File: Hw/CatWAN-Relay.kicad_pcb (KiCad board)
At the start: 2 copper layers, 50 x 86.9 mm, 55 parts, among them J2 INPUTS, J3 OUTPUTS, J4 I2C, J5 Serial, P1 USB_C_Plug_USB2.0, Q1 MMBT2222A, Q2 MMBT2222A, Q3 MMBT2222A, SW1 BOOT, SW2 RESET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

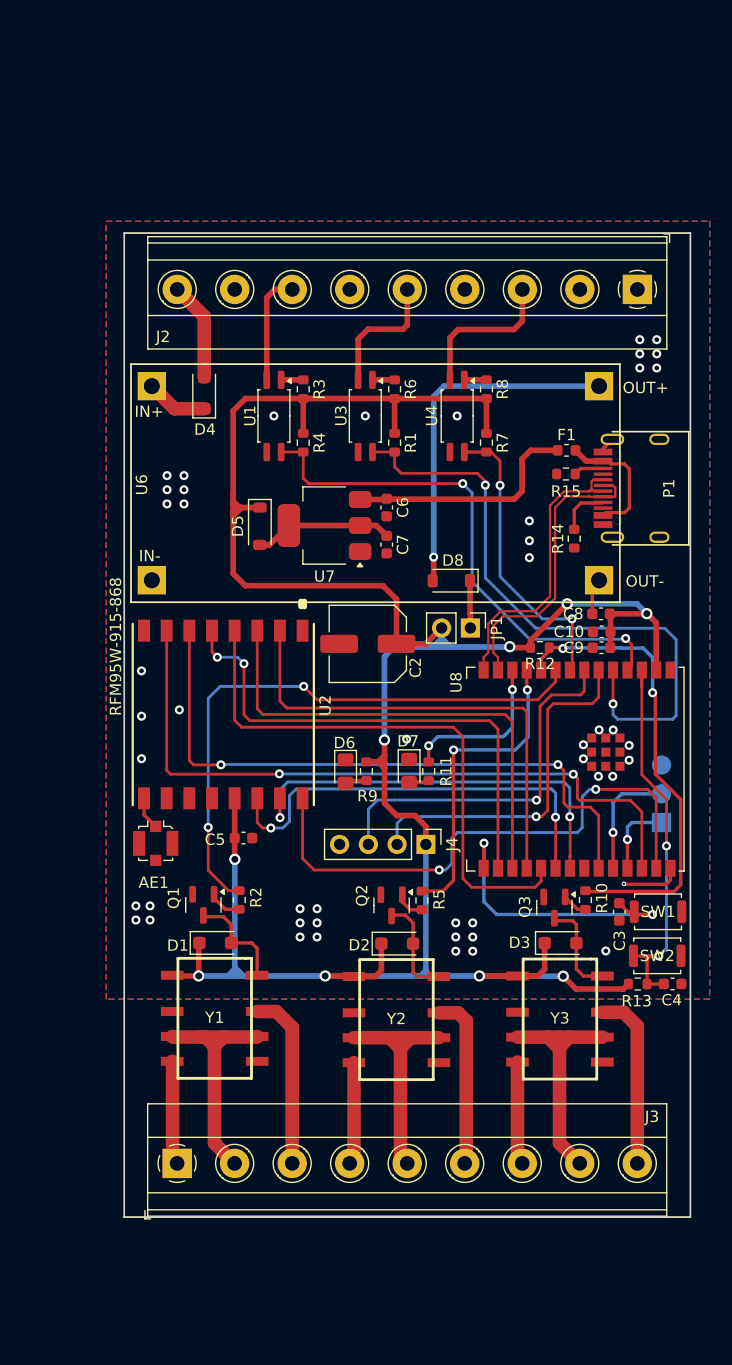
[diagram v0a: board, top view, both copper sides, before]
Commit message: feat(hw): add labels in PCB design
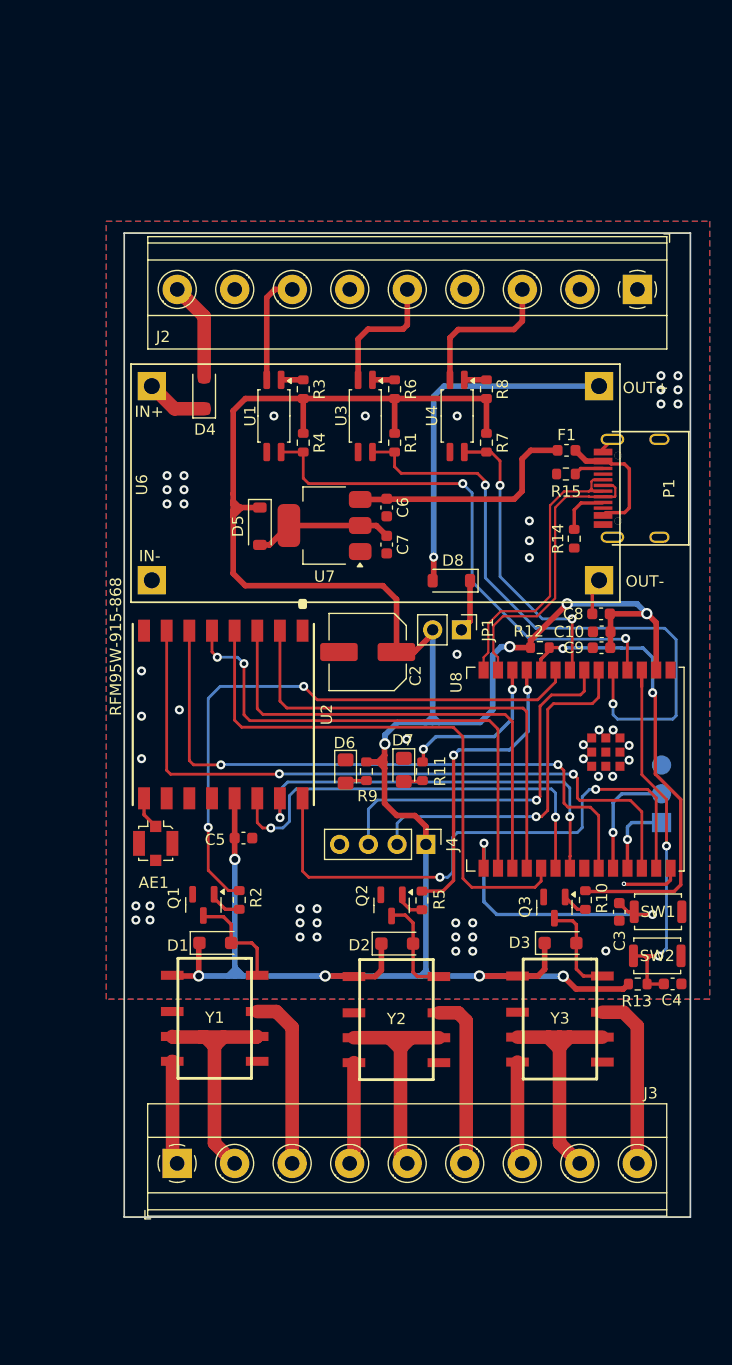
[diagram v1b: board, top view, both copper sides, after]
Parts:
- added G***: LOGO, agroin:electronic_cats_logo_8x6, B.Cu at (55.7, 67.0)
- added kibuzzard-67649598: G***, kibuzzard-67649598, B.Cu at (85.9, 89.6)
- added kibuzzard-676495AB: G***, kibuzzard-676495AB, B.Cu at (85.9, 87.1)
- added kibuzzard-676D7180: G***, kibuzzard-676D7180, B.Cu at (85.6, 84.6)
- added kibuzzard-676D7534: G***, kibuzzard-676D7534, B.Cu at (79.7, 51.0)
- added kibuzzard-676D753C: G***, kibuzzard-676D753C, B.Cu at (79.5, 68.1)
- added kibuzzard-676D7543: G***, kibuzzard-676D7543, B.Cu at (47.2, 68.2)
- added kibuzzard-676D7549: G***, kibuzzard-676D7549, B.Cu at (47.2, 51.2)
- added kibuzzard-676D7550: G***, kibuzzard-676D7550, B.Cu at (46.1, 115.3)
- added kibuzzard-676D7558: G***, kibuzzard-676D7558, B.Cu at (51.2, 115.0)
- added kibuzzard-676D7562: G***, kibuzzard-676D7562, B.Cu at (56.2, 115.3)
- added kibuzzard-676D7567: G***, kibuzzard-676D7567, B.Cu at (61.3, 115.3)
- added kibuzzard-676D757C: G***, kibuzzard-676D757C, B.Cu at (71.6, 115.3)
- added kibuzzard-676D7581: G***, kibuzzard-676D7581, B.Cu at (76.7, 115.3)
- added kibuzzard-676D758E: G***, kibuzzard-676D758E, B.Cu at (86.9, 115.3)
- added kibuzzard-676D75AF: G***, kibuzzard-676D75AF, B.Cu at (66.4, 114.8)
- added kibuzzard-676D75BA: G***, kibuzzard-676D75BA, B.Cu at (81.8, 114.8)
- added kibuzzard-676D829F: G***, kibuzzard-676D829F, B.Cu at (62.0, 67.0)
- added kibuzzard-676D82E6: G***, kibuzzard-676D82E6, B.Cu at (46.1, 47.0)
- added kibuzzard-676D82FB: G***, kibuzzard-676D82FB, B.Cu at (51.2, 47.0)
- added kibuzzard-676D8308: G***, kibuzzard-676D8308, B.Cu at (56.3, 46.5)
- added kibuzzard-676D8313: G***, kibuzzard-676D8313, B.Cu at (61.4, 47.0)
- added kibuzzard-676D831D: G***, kibuzzard-676D831D, B.Cu at (66.5, 46.4)
- added kibuzzard-676D8326: G***, kibuzzard-676D8326, B.Cu at (71.5, 47.0)
- added kibuzzard-676D832F: G***, kibuzzard-676D832F, B.Cu at (76.6, 46.5)
- added kibuzzard-676D8337: G***, kibuzzard-676D8337, B.Cu at (81.7, 47.0)
- added kibuzzard-676D833E: G***, kibuzzard-676D833E, B.Cu at (86.8, 47.0)
- moved JP1 0.81 mm to (71.2, 72.6)
- moved C2 0.72 mm to (63.0, 74.6)
- moved R11 0.55 mm to (67.8, 85.1)
- moved D7 0.48 mm to (66.2, 85.0)
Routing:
- net +3V3: track 229.9 -> 233.8 mm
- net /DIO2: track 49.4 -> 51.0 mm
- net /DO2: track 27.7 -> 27.2 mm
- net GND: vias 49 -> 50

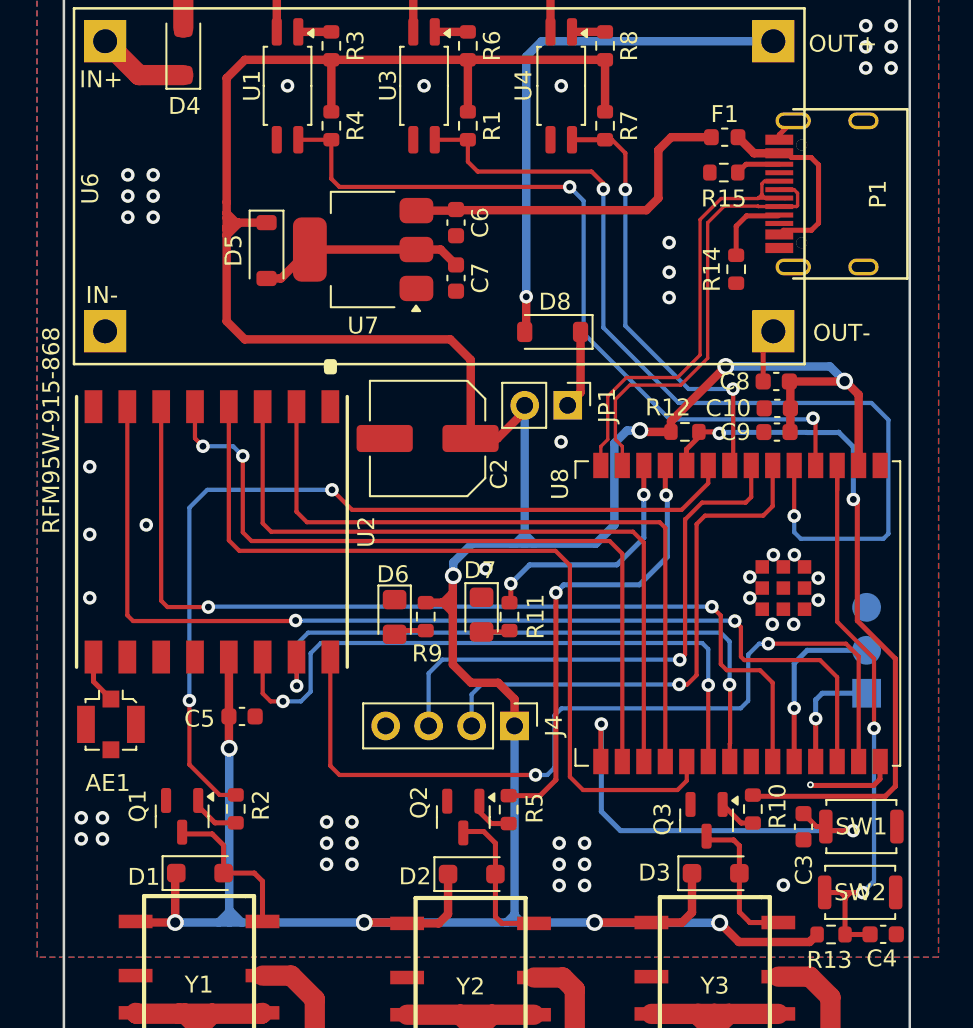
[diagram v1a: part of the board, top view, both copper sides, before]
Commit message: feat(Hw):Update_Tracks
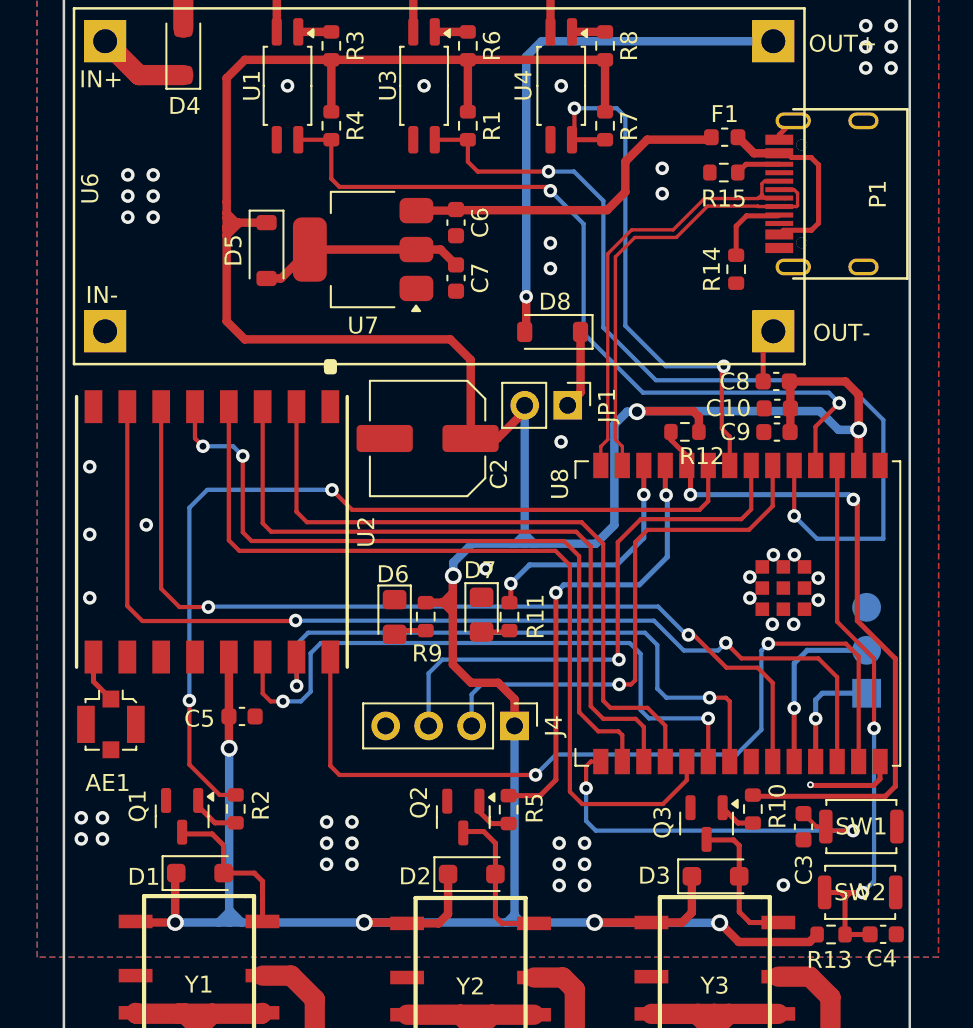
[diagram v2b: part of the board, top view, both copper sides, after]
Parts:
- moved Q3 0.19 mm to (79.5, 97.3)
- moved D3 0.18 mm to (80.0, 100.5)
- turned R12 to 0 degrees
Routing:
- net /DI1: track 26.2 -> 32.4 mm
- net +3V3: track 233.8 -> 238.4 mm, vias 9 -> 8
- net /BOOT: track 26.1 -> 23.6 mm
- net /RFM_RST: track 56.0 -> 53.9 mm
- net /DI3: track 46.1 -> 47.8 mm
- net /DI2: track 56.0 -> 54.4 mm
- net /MISO: track 42.2 -> 40.8 mm
- net /SCK: track 49.8 -> 51.0 mm
- net /DO1: track 41.6 -> 40.6 mm
- net /DIO5: track 61.8 -> 60.9 mm
- net /SS: track 45.0 -> 44.1 mm
- net /MOSI: track 42.8 -> 42.0 mm
- net /DIO2: track 51.0 -> 50.4 mm
- net /DO3: track 52.0 -> 52.6 mm
- net VBUS: track 20.9 -> 20.3 mm
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
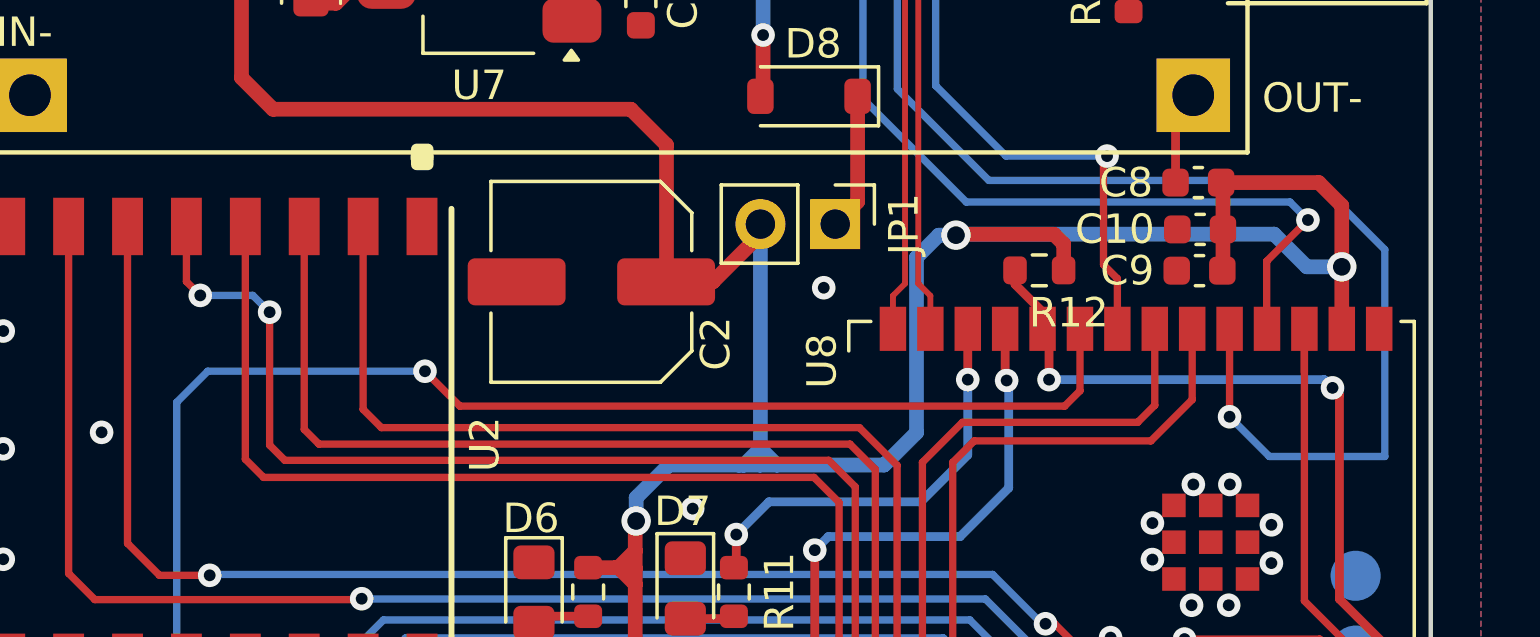
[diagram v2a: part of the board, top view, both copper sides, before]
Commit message: feat(Hw):added_labels
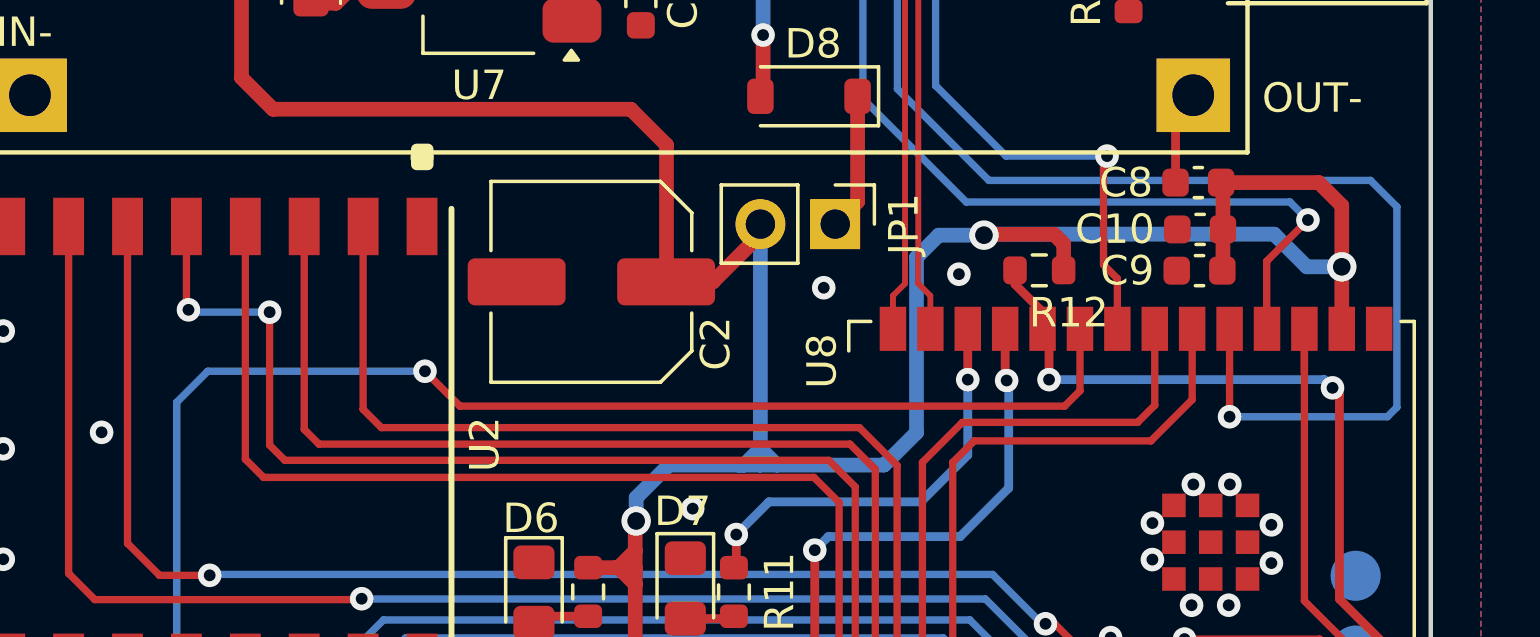
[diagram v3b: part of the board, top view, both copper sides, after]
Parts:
- added kibuzzard-677EAF7D: G***, kibuzzard-677EAF7D, B.Cu at (65.6, 94.3)
- added kibuzzard-677EAF9B: G***, kibuzzard-677EAF9B, B.Cu at (63.0, 94.4)
- added kibuzzard-677EAFAE: G***, kibuzzard-677EAFAE, B.Cu at (60.5, 94.2)
- added kibuzzard-677EAFBC: G***, kibuzzard-677EAFBC, B.Cu at (68.2, 94.3)
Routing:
- net +3V3: track 238.4 -> 237.5 mm
- net /SS: track 44.1 -> 44.6 mm
- net GND: vias 51 -> 52

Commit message: feat: files_modified, _pro, _pcb & _sch
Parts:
- removed G***: LOGO, agroin:electronic_cats_logo_8x6
- removed kibuzzard-67649598: G***, kibuzzard-67649598
- removed kibuzzard-676495AB: G***, kibuzzard-676495AB
- removed kibuzzard-676D7180: G***, kibuzzard-676D7180
- removed kibuzzard-676D7534: G***, kibuzzard-676D7534
- removed kibuzzard-676D753C: G***, kibuzzard-676D753C
- removed kibuzzard-676D7543: G***, kibuzzard-676D7543
- removed kibuzzard-676D7549: G***, kibuzzard-676D7549
- removed kibuzzard-676D7550: G***, kibuzzard-676D7550
- removed kibuzzard-676D7558: G***, kibuzzard-676D7558
- removed kibuzzard-676D7562: G***, kibuzzard-676D7562
- removed kibuzzard-676D7567: G***, kibuzzard-676D7567
- removed kibuzzard-676D757C: G***, kibuzzard-676D757C
- removed kibuzzard-676D7581: G***, kibuzzard-676D7581
- removed kibuzzard-676D758E: G***, kibuzzard-676D758E
- removed kibuzzard-676D75AF: G***, kibuzzard-676D75AF
- removed kibuzzard-676D75BA: G***, kibuzzard-676D75BA
- removed kibuzzard-676D829F: G***, kibuzzard-676D829F
- removed kibuzzard-676D82E6: G***, kibuzzard-676D82E6
- removed kibuzzard-676D82FB: G***, kibuzzard-676D82FB
- removed kibuzzard-676D8308: G***, kibuzzard-676D8308
- removed kibuzzard-676D8313: G***, kibuzzard-676D8313
- removed kibuzzard-676D831D: G***, kibuzzard-676D831D
- removed kibuzzard-676D8326: G***, kibuzzard-676D8326
- removed kibuzzard-676D832F: G***, kibuzzard-676D832F
- removed kibuzzard-676D8337: G***, kibuzzard-676D8337
- removed kibuzzard-676D833E: G***, kibuzzard-676D833E
- removed kibuzzard-677EAF7D: G***, kibuzzard-677EAF7D
- removed kibuzzard-677EAF9B: G***, kibuzzard-677EAF9B
- removed kibuzzard-677EAFAE: G***, kibuzzard-677EAFAE
- removed kibuzzard-677EAFBC: G***, kibuzzard-677EAFBC
- added J1: Conn_01x01, Connector_PinHeader_2.54mm:PinHeader_1x01_P2.54mm_Vertical, F.Cu at (57.0, 70.0)
- D7: value Rx -> SS0_LED
- J4: footprint Connector_PinHeader_2.54mm:PinHeader_1x04_P2.54mm_Vertical -> Connector_PinHeader_2.54mm:PinHeader_1x06_P2.54mm_Vertical
- J5: moved to F.Cu
- U8: footprint PCM_Espressif:ESP32-C6-WROOM-1U -> Espressif:ESP32-C6-WROOM-1U
- moved C5 35.1 mm to (45.5, 56.5), turned to 180 degrees
- moved J4 28.8 mm to (78.0, 64.5)
- moved R12 28.4 mm to (76.5, 102.5), turned to -90 degrees
- moved D8 26.1 mm to (64.0, 43.0), turned to 0 degrees
- moved R14 25.4 mm to (69.5, 42.0)
- moved R15 21.4 mm to (72.5, 39.0), turned to -90 degrees
- moved C2 20.4 mm to (53.5, 56.5), turned to 0 degrees
- moved C7 19.9 mm to (54.5, 48.0), turned to 90 degrees
- moved P1 19.9 mm to (75.4, 42.5)
- moved C8 19.5 mm to (75.5, 53.5), turned to 0 degrees
- moved J2 19.4 mm to (78.6, 25.0)
- moved R3 19.3 mm to (51.5, 33.0)
- moved C10 19.1 mm to (75.5, 55.5), turned to 0 degrees
- moved U6 19.0 mm to (35.0, 31.6)
- moved U1 18.8 mm to (48.5, 36.0)
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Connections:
- net /SS renamed /SS0
- J4 pad 4: GND -> /<NO NET>
- R11 pad 1: /RX_LED -> /SS1
- U8 pad 12: /RX_LED -> /SS1
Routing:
- net +3V3: track 237.5 -> 285.1 mm, vias 8 -> 11
- net /SCL: track 33.0 -> 4.82 mm, vias 1 -> 0
- net /DI2: track 53.9 -> 80.3 mm, vias 2 -> 3
- net /SDA: track 31.5 -> 5.20 mm, vias 1 -> 0
- net /SS1: track 0.00 -> 25.1 mm, vias 0 -> 1
- net Net-(D8-K): track 4.65 -> 29.3 mm, vias 0 -> 2
- net /SCK: track 51.0 -> 33.0 mm, vias 0 -> 2
- net /DO1: track 40.6 -> 58.1 mm, vias 2 -> 1
- net /DI1: track 32.4 -> 48.8 mm
- net Net-(D8-A): track 31.3 -> 15.3 mm, vias 1 -> 2
- net /RX_LED: track 14.4 -> 0.00 mm, vias 2 -> 0
- net /DIO2: track 50.4 -> 36.0 mm
- net VBUS: track 20.3 -> 6.03 mm
- net /MOSI: track 42.0 -> 30.1 mm, vias 0 -> 2
- net /SS0: track 44.6 -> 32.9 mm
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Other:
- board size 50 x 86.9 mm -> 47.5 x 115.5 mm

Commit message: feat: fix pcb
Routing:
- net GND: track 0.00 -> 0.05 mm, vias 0 -> 34
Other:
- board size 47.5 x 115.5 mm -> 49.5 x 115.5 mm
